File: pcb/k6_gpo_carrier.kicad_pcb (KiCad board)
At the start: 2 copper layers, 100 x 80 mm, 22 parts, among them J1 LM2596_Buck, J10 BTN_RESET, J2 XL6009_Boost, J3 12V_IN, J4 PHONE, J5 MAX98357A, J6 DAC_OUT, J7 SD_Card, J8 BTN_RING, J9 BTN_CANCEL, T1 600R_XFMR, U1 ESP32_DevKit, U2 L293D, U3 PC817

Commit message: fix: Unique reference designators for mounting holes (MH1-MH4)
FreeRouting/Specctra export requires unique reference designators.
All four mounting holes now have MH1, MH2, MH3, MH4 instead of
all sharing 'MH'.

Co-Authored-By: Devin AI <158243242+devin-ai-integration[bot]@users.noreply.github.com>
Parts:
- removed MH (x4): MH, K6_GPO:MH
- added MH1: MH, K6_GPO:MH1, F.Cu at (134.0, 94.0)
- added MH2: MH, K6_GPO:MH2, F.Cu at (226.0, 94.0)
- added MH3: MH, K6_GPO:MH3, F.Cu at (134.0, 166.0)
- added MH4: MH, K6_GPO:MH4, F.Cu at (226.0, 166.0)
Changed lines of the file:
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@@
   (gr_line (start 230.000 170.000) (end 130.000 170.000) (stroke (width 0.1) (type default)) (layer "Edge.Cuts"))
   (gr_line (start 130.000 170.000) (end 130.000 90.000) (stroke (width 0.1) (type default)) (layer "Edge.Cuts"))
-  (footprint "K6_GPO:MH" (layer "F.Cu")
+  (footprint "K6_GPO:MH1" (layer "F.Cu")
     (at 134.000 94.000 0)
-      (fp_text reference "MH" (at 0.000 -2.000) (layer "F.SilkS")
+      (fp_text reference "MH1" (at 0.000 -2.000) (layer "F.SilkS")
     (effects (font (size 1 1) (thickness 0.15)))
 )
@@
   (pad "" np_thru_hole circle (at 0.000 0.000) (size 3.2 3.2) (drill 3.2) (layers "*.Cu" "*.Mask"))
   )
-  (footprint "K6_GPO:MH" (layer "F.Cu")
+  (footprint "K6_GPO:MH2" (layer "F.Cu")
     (at 226.000 94.000 0)
-      (fp_text reference "MH" (at 0.000 -2.000) (layer "F.SilkS")
+      (fp_text reference "MH2" (at 0.000 -2.000) (layer "F.SilkS")
     (effects (font (size 1 1) (thickness 0.15)))
 )
@@
   (pad "" np_thru_hole circle (at 0.000 0.000) (size 3.2 3.2) (drill 3.2) (layers "*.Cu" "*.Mask"))
   )
-  (footprint "K6_GPO:MH" (layer "F.Cu")
+  (footprint "K6_GPO:MH3" (layer "F.Cu")
     (at 134.000 166.000 0)
-      (fp_text reference "MH" (at 0.000 -2.000) (layer "F.SilkS")
+      (fp_text reference "MH3" (at 0.000 -2.000) (layer "F.SilkS")
     (effects (font (size 1 1) (thickness 0.15)))
 )
@@
   (pad "" np_thru_hole circle (at 0.000 0.000) (size 3.2 3.2) (drill 3.2) (layers "*.Cu" "*.Mask"))
   )
-  (footprint "K6_GPO:MH" (layer "F.Cu")
+  (footprint "K6_GPO:MH4" (layer "F.Cu")
     (at 226.000 166.000 0)
-      (fp_text reference "MH" (at 0.000 -2.000) (layer "F.SilkS")
+      (fp_text reference "MH4" (at 0.000 -2.000) (layer "F.SilkS")
     (effects (font (size 1 1) (thickness 0.15)))
 )

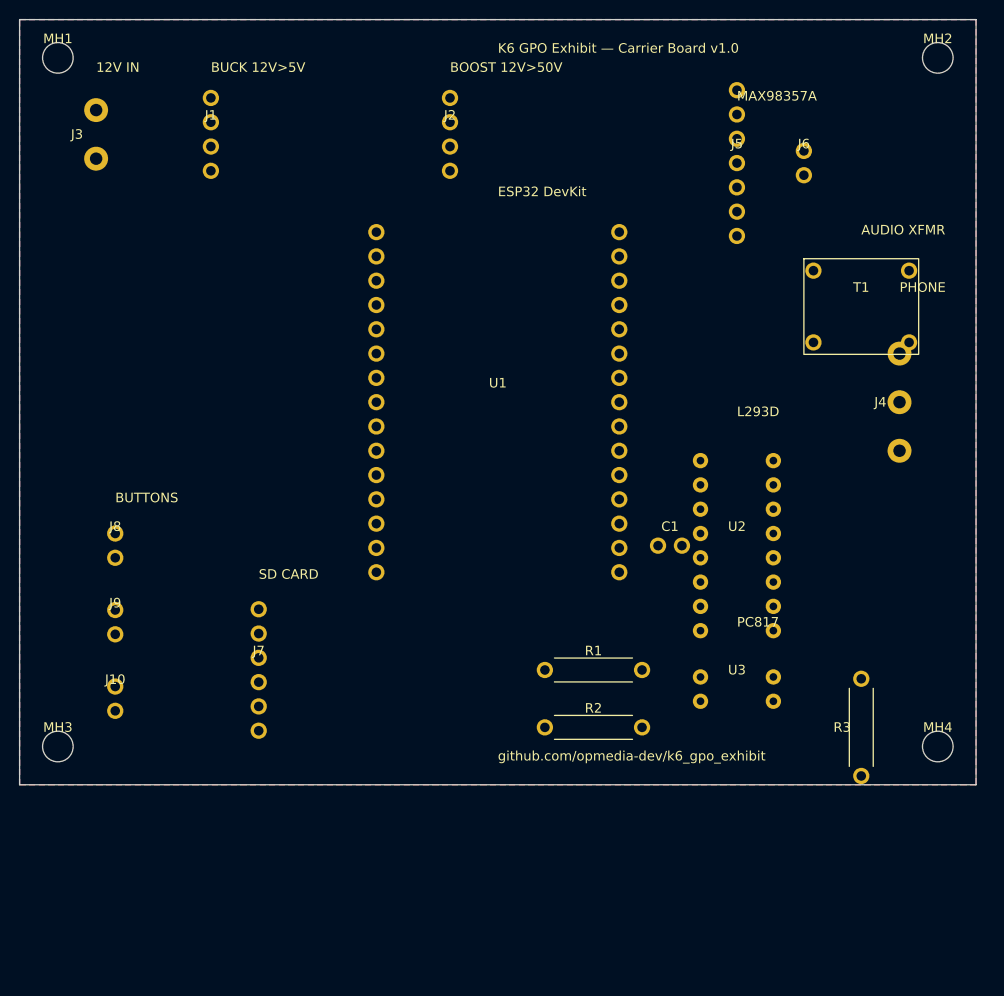
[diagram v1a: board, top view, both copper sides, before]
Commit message: feat: Add detailed pin labels to silkscreen for all connectors
Every connector now has per-pin silkscreen labels showing:
- J3: 12V IN (+12V, GND)
- J1: Buck converter (IN+/IN-/OUT+/OUT-)
- J2: Boost converter (IN+/IN-/OUT+/OUT-)
- U1: ESP32 DevKit (all 30 GPIO labels with function names)
- J5: MAX98357A DAC (VIN, GND, SD, GAIN, DIN, BCLK, LRC)
- J6: DAC output (SPK+, SPK-)
- J4: Phone cord (LINE A Red, LINE B White, BELL Blue)
- J7: SD Card (GND, VCC, MOSI, MISO, SCK, CS)
- J8/J9/J10: Buttons (RING/CANCEL/RESET + GND)
- U2: L293D (all 16 pins with net connections)
- U3: PC817 (Anode, Cathode, Emitter, Collector)
- T1: Audio transformer (P1/P2 speaker, S1/S2 line)
- R1, R2, R3, C1: Values and connections

Co-Authored-By: Devin AI <158243242+devin-ai-integration[bot]@users.noreply.github.com>
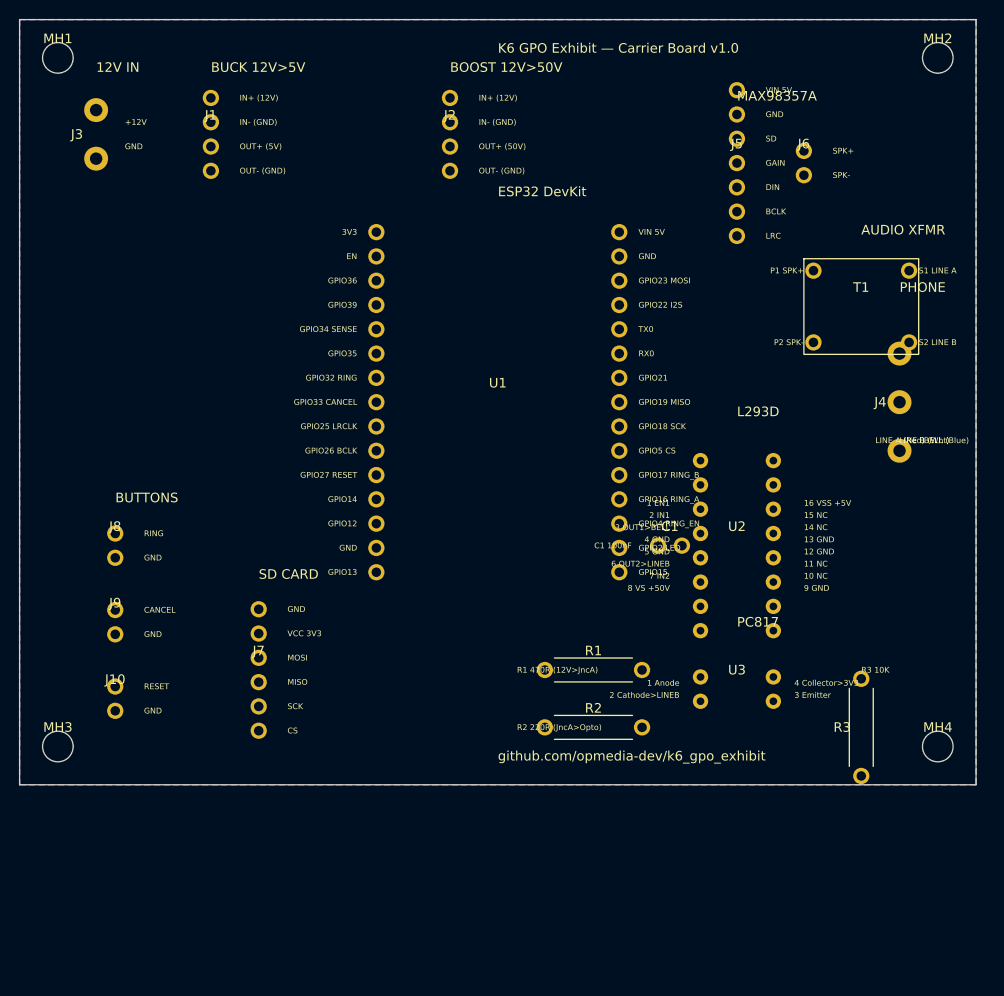
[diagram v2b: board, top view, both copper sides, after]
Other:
- board text added: "+12V"
- board text added: "1 Anode"
- board text added: "1 EN1"
- board text added: "10 NC"
- board text added: "11 NC"
- board text added: "12 GND"
- board text added: "13 GND"
- board text added: "14 NC"
- board text added: "15 NC"
- board text added: "16 VSS +5V"
- board text added: "2 Cathode>LINEB"
- board text added: "2 IN1"
- board text added: "3 Emitter"
- board text added: "3 OUT1>BELL"
- board text added: "3V3"
- board text added: "4 Collector>3V3"
- board text added: "4 GND"
- board text added: "5 GND"
- board text added: "6 OUT2>LINEB"
- board text added: "7 IN2"
- board text added: "8 VS +50V"
- board text added: "9 GND"
- board text added: "BCLK"
- board text added: "BELL (Blue)"
- board text added: "C1 100nF"
- board text added: "CANCEL"
- board text added: "CS"
- board text added: "DIN"
- board text added: "EN"
- board text added: "GAIN"
- board text added: "GND"
- board text added: "GPIO12"
- board text added: "GPIO13"
- board text added: "GPIO14"
- board text added: "GPIO15"
- board text added: "GPIO16 RING_A"
- board text added: "GPIO17 RING_B"
- board text added: "GPIO18 SCK"
- board text added: "GPIO19 MISO"
- board text added: "GPIO2 LED"
- board text added: "GPIO21"
- board text added: "GPIO22 I2S"
- board text added: "GPIO23 MOSI"
- board text added: "GPIO25 LRCLK"
- board text added: "GPIO26 BCLK"
- board text added: "GPIO27 RESET"
- board text added: "GPIO32 RING"
- board text added: "GPIO33 CANCEL"
- board text added: "GPIO34 SENSE"
- board text added: "GPIO35"
- board text added: "GPIO36"
- board text added: "GPIO39"
- board text added: "GPIO4 RING_EN"
- board text added: "GPIO5 CS"
- board text added: "IN+ (12V)"
- board text added: "IN- (GND)"
- board text added: "LINE A (Red)"
- board text added: "LINE B (Wht)"
- board text added: "LRC"
- board text added: "MISO"
- board text added: "MOSI"
- board text added: "OUT+ (50V)"
- board text added: "OUT+ (5V)"
- board text added: "OUT- (GND)"
- board text added: "P1 SPK+"
- board text added: "P2 SPK-"
- board text added: "R1 470R (12V>JncA)"
- board text added: "R2 220R (JncA>Opto)"
- board text added: "R3 10K"
- board text added: "RESET"
- board text added: "RING"
- board text added: "RX0"
- board text added: "S1 LINE A"
- board text added: "S2 LINE B"
- board text added: "SCK"
- board text added: "SD"
- board text added: "SPK+"
- board text added: "SPK-"
- board text added: "TX0"
- board text added: "VCC 3V3"
- board text added: "VIN 5V"

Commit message: fix: Resolve label overlap — enlarge board to 100x100mm, shorten labels, add pinout reference
- Board enlarged from 100x80mm to 100x100mm (still JLCPCB cheapest tier)
- Components repositioned with more spacing between zones
- Silkscreen labels shortened (e.g. GPIO34 SENSE → 34 SN)
- Fixed L293D/PC817 label pitch (was 1.27mm, corrected to 2.54mm)
- Added pcb/PINOUT.md with complete pinout tables for every connector
- Updated README with new board dimensions and layout diagram

Co-Authored-By: Devin AI <158243242+devin-ai-integration[bot]@users.noreply.github.com>
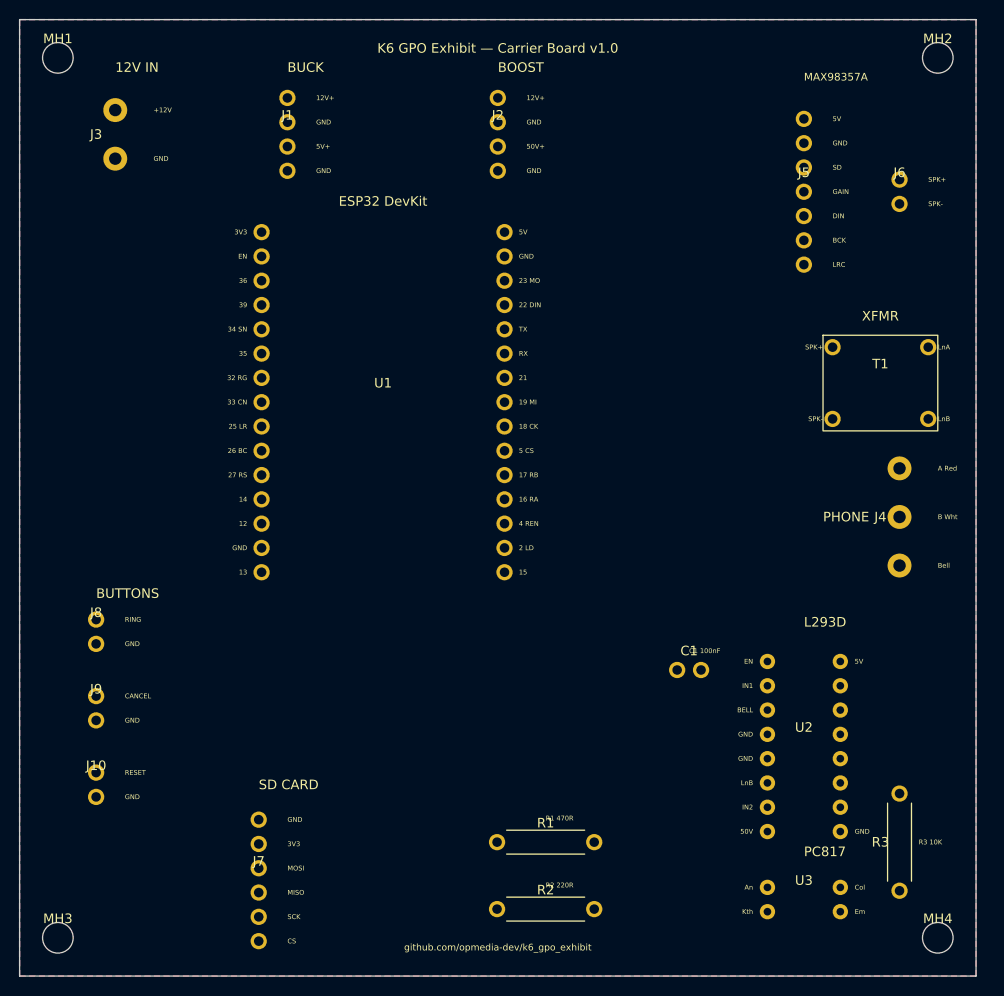
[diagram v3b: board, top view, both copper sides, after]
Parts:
- moved U3 23.1 mm to (212.0, 182.0)
- moved U2 22.1 mm to (212.0, 166.0)
- moved J7 22.0 mm to (155.0, 180.0)
- moved MH3 20.0 mm to (134.0, 186.0)
- moved MH4 20.0 mm to (226.0, 186.0)
- moved R2 19.6 mm to (185.0, 183.0)
- moved R1 18.7 mm to (185.0, 176.0)
- moved C1 13.2 mm to (200.0, 158.0)
- moved R3 12.6 mm to (222.0, 176.0)
- moved J4 12.0 mm to (222.0, 142.0)
- moved U1 12.0 mm to (168.0, 130.0)
- moved J6 10.4 mm to (222.0, 108.0)
- moved J10 9.22 mm to (138.0, 170.0)
- moved J8 9.22 mm to (138.0, 154.0)
- moved J9 9.22 mm to (138.0, 162.0)
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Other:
- board size 100 x 80 mm -> 100 x 100 mm
- board text added: "12"
- board text added: "12V+"
- board text added: "13"
- board text added: "14"
- board text added: "15"
- board text added: "16 RA"
- board text added: "17 RB"
- board text added: "18 CK"
- board text added: "19 MI"
- board text added: "2 LD"
- board text added: "21"
- board text added: "22 DIN"
- board text added: "23 MO"
- board text added: "25 LR"
- board text added: "26 BC"
- board text added: "27 RS"
- board text added: "32 RG"
- board text added: "33 CN"
- board text added: "34 SN"
- board text added: "35"
- board text added: "36"
- board text added: "39"
- board text added: "4 REN"
- board text added: "5 CS"
- board text added: "50V"
- board text added: "50V+"
- board text added: "5V"
- board text added: "5V+"
- board text added: "A Red"
- board text added: "An"
- board text added: "B Wht"
- board text added: "BCK"
- board text added: "BELL"
- board text added: "BOOST"
- board text added: "BUCK"
- board text added: "Bell"
- board text added: "Col"
- board text added: "Em"
- board text added: "IN1"
- board text added: "IN2"
- board text added: "Kth"
- board text added: "LnA"
- board text added: "LnB"
- board text added: "R1 470R"
- board text added: "R2 220R"
- board text added: "RX"
- board text added: "TX"
- board text added: "XFMR"
- board text removed: "1 Anode"
- board text removed: "1 EN1"
- board text removed: "10 NC"
- board text removed: "11 NC"
- board text removed: "12 GND"
- board text removed: "13 GND"
- board text removed: "14 NC"
- board text removed: "15 NC"
- board text removed: "16 VSS +5V"
- board text removed: "2 Cathode>LINEB"
- board text removed: "2 IN1"
- board text removed: "3 Emitter"
- board text removed: "3 OUT1>BELL"
- board text removed: "4 Collector>3V3"
- board text removed: "4 GND"
- board text removed: "5 GND"
- board text removed: "6 OUT2>LINEB"
- board text removed: "7 IN2"
- board text removed: "8 VS +50V"
- board text removed: "9 GND"
- board text removed: "AUDIO XFMR"
- board text removed: "BCLK"
- board text removed: "BELL (Blue)"
- board text removed: "BOOST 12V>50V"
- board text removed: "BUCK 12V>5V"
- board text removed: "GPIO12"
- board text removed: "GPIO13"
- board text removed: "GPIO14"
- board text removed: "GPIO15"
- board text removed: "GPIO16 RING_A"
- board text removed: "GPIO17 RING_B"
- board text removed: "GPIO18 SCK"
- board text removed: "GPIO19 MISO"
- board text removed: "GPIO2 LED"
- board text removed: "GPIO21"
- board text removed: "GPIO22 I2S"
- board text removed: "GPIO23 MOSI"
- board text removed: "GPIO25 LRCLK"
- board text removed: "GPIO26 BCLK"
- board text removed: "GPIO27 RESET"
- board text removed: "GPIO32 RING"
- board text removed: "GPIO33 CANCEL"
- board text removed: "GPIO34 SENSE"
- board text removed: "GPIO35"
- board text removed: "GPIO36"
- board text removed: "GPIO39"
- board text removed: "GPIO4 RING_EN"
- board text removed: "GPIO5 CS"
- board text removed: "IN+ (12V)"
- board text removed: "IN- (GND)"
- board text removed: "LINE A (Red)"
- board text removed: "LINE B (Wht)"
- board text removed: "OUT+ (50V)"
- board text removed: "OUT+ (5V)"
- board text removed: "OUT- (GND)"
- board text removed: "P1 SPK+"
- board text removed: "P2 SPK-"
- board text removed: "R1 470R (12V>JncA)"
- board text removed: "R2 220R (JncA>Opto)"
- board text removed: "RX0"
- board text removed: "S1 LINE A"
- board text removed: "S2 LINE B"
- board text removed: "TX0"
- board text removed: "VCC 3V3"
- board text removed: "VIN 5V"
